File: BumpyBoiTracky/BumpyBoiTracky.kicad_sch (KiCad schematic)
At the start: 0 parts

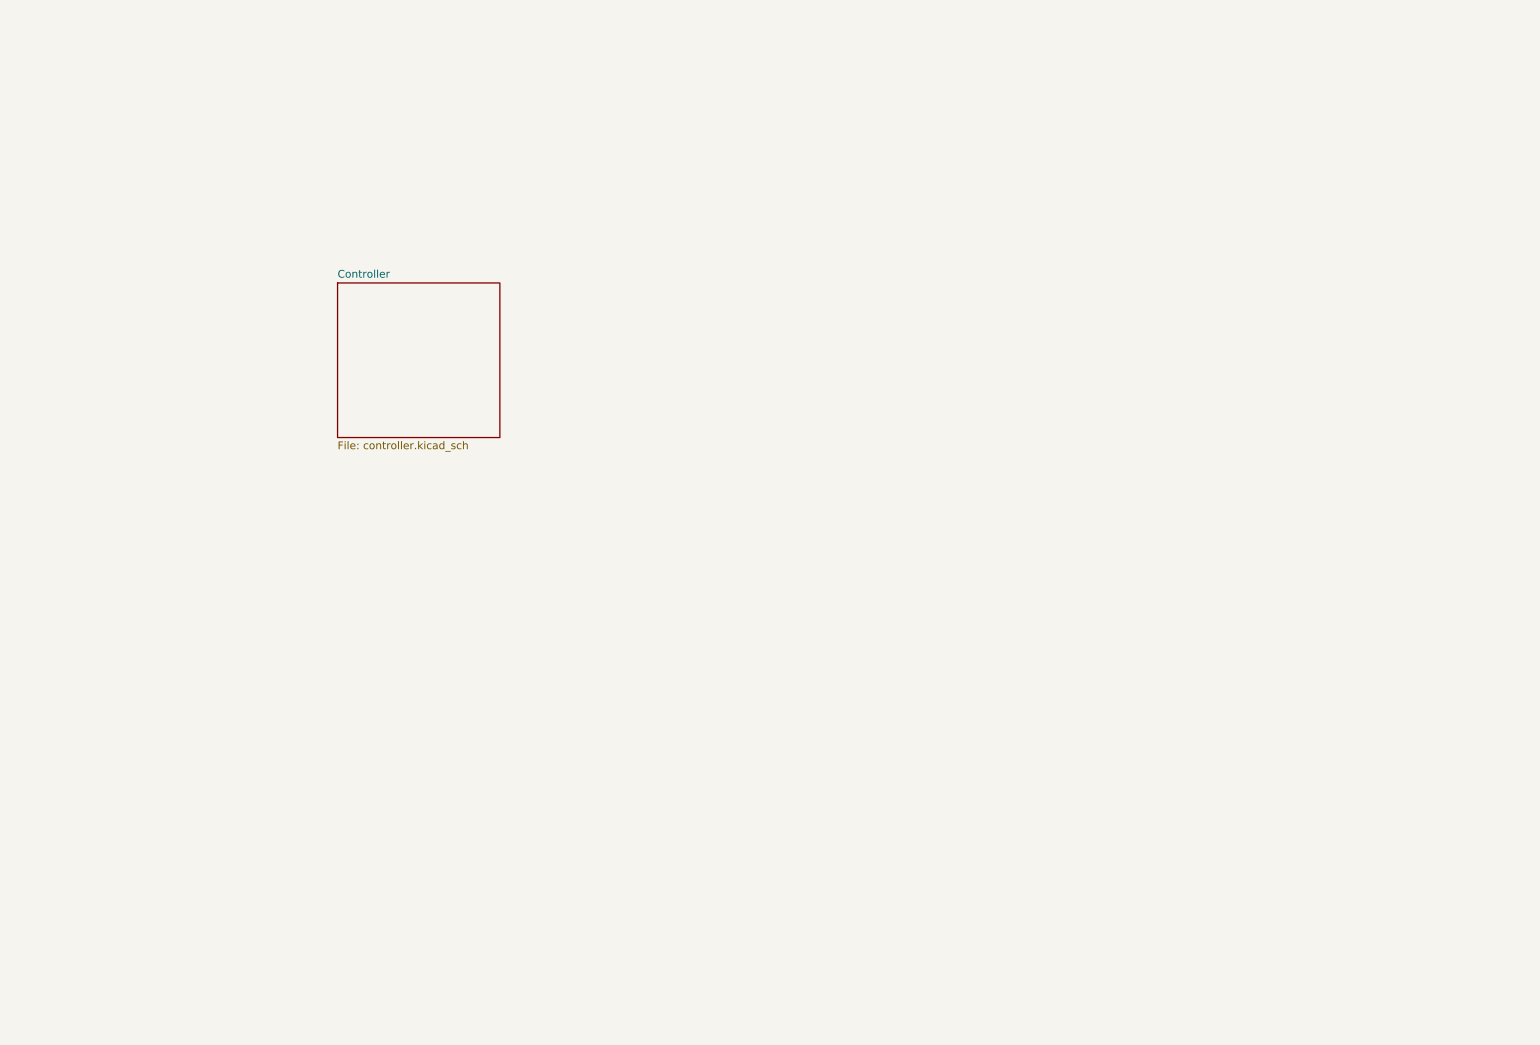
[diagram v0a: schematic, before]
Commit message: Controller Added
Added controller and Sensor. Begun work on prog interface
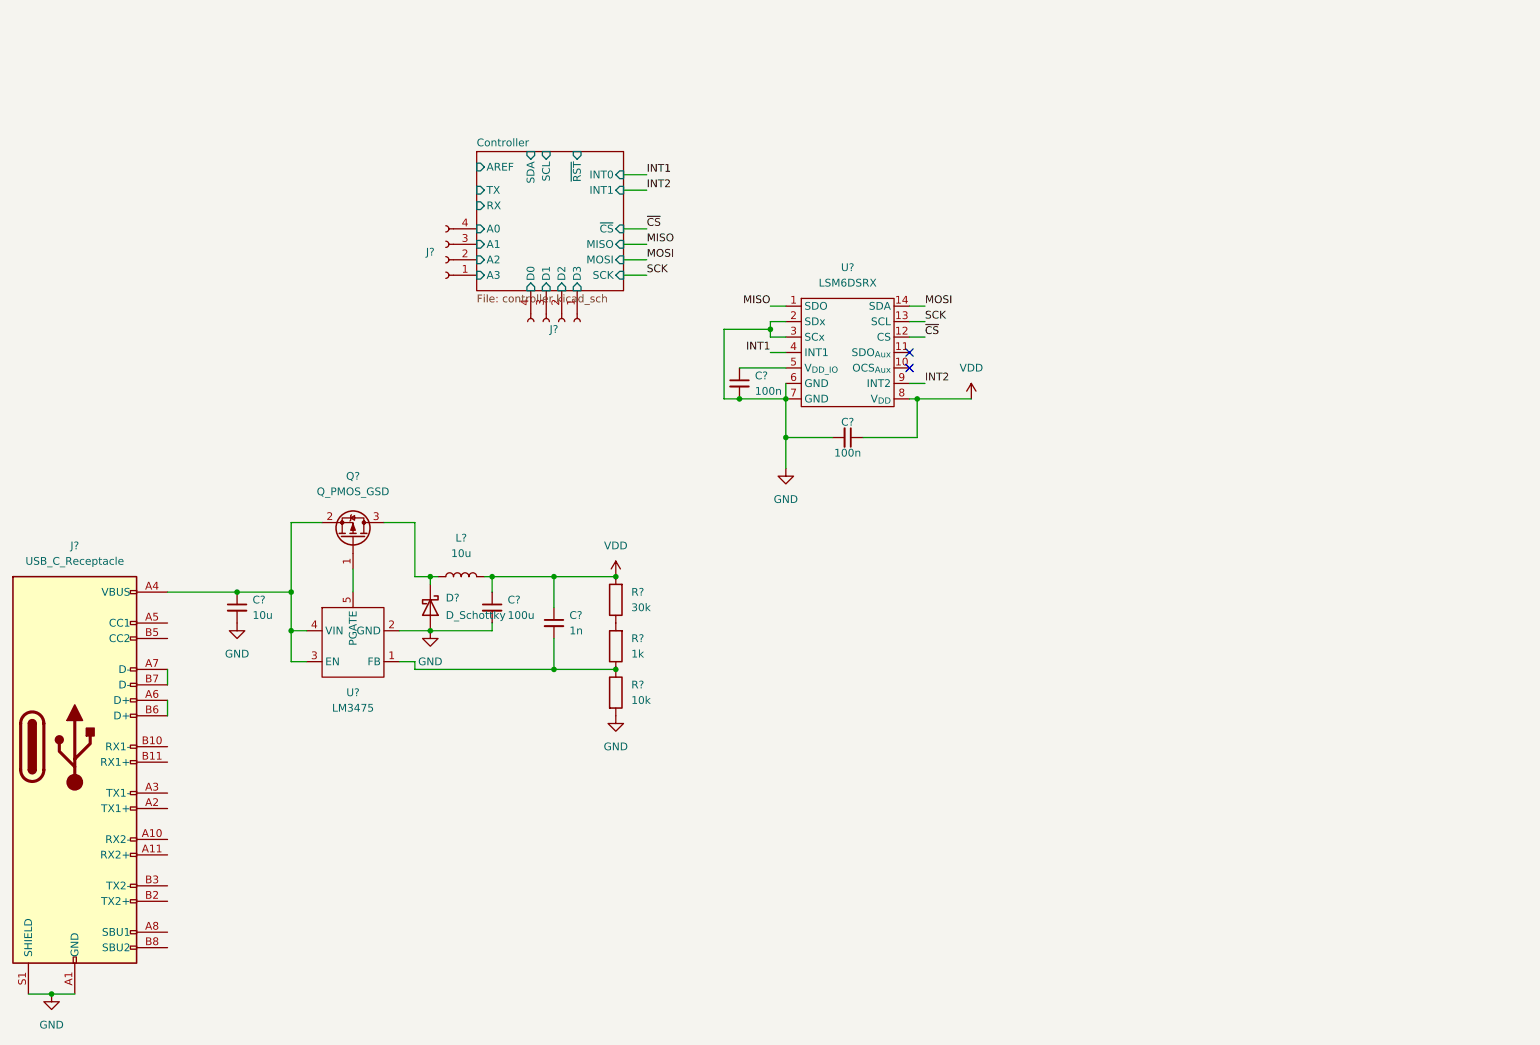
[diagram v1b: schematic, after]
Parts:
- added C?: 1n, symbol Device:C_Small
- added C? (x2): 100n, symbol Device:C_Small
- added C?: 100u, symbol Device:C_Small
- added C?: 10u, symbol Device:C_Small
- added D?: D_Schottky, symbol Device:D_Schottky
- added J?: USB_C_Receptacle, symbol Connector:USB_C_Receptacle
- added J? (x2): Conn_01x04_Female, symbol Connector:Conn_01x04_Female
- added L?: 10u, symbol Device:L
- added Q?: Q_PMOS_GSD, symbol Device:Q_PMOS_GSD
- added R?: 30k, symbol Device:R
- added R?: 1k, symbol Device:R
- added R?: 10k, symbol Device:R
- added U?: LM3475, Package_TO_SOT_SMD:SOT-23-5, symbol BumpyBoiTracky:LM3475
- added U?: LSM6DSRX, BumpyBoiTracky:LGA-14L, symbol BumpyBoiTracky:LSM6DSRX
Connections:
- new net: R?.1, R?.2
- new net: C?.2, R?.1, R?.1, U?.1 (FB)
- new net: C?.1, U?.5 (V_{DD_IO})
- new net: C?.1, J?.A4 (VBUS), J?.A9 (VBUS), J?.B4 (VBUS), J?.B9 (VBUS), Q?.2 (S), U?.3 (EN), U?.4 (VIN)
- new net: Q?.1 (G), U?.5 (PGATE)
- new net: D?.1 (K), L?.1, Q?.3 (D)
- new net: J?.A6 (D+), J?.B6 (D+)
- new net: J?.A7 (D-), J?.B7 (D-)
- new net Controller/A0: J?.4 (Pin_4)
- new net Controller/A1: J?.3 (Pin_3)
- new net Controller/A2: J?.2 (Pin_2)
- new net Controller/A3: J?.1 (Pin_1)
- new net Controller/D0: J?.4 (Pin_4)
- new net Controller/D1: J?.3 (Pin_3)
- new net Controller/D2: J?.2 (Pin_2)
- new net Controller/D3: J?.1 (Pin_1)
- new net GND: C?.2, C?.2, C?.2, C?.2, D?.2 (A), J?.A1 (GND), J?.A12 (GND), J?.B1 (GND), J?.B12 (GND), J?.S1 (SHIELD), R?.2, U?.2 (GND), U?.2 (SDx), U?.3 (SCx), U?.6 (GND), U?.7 (GND)
- new net INT1: U?.4 (INT1)
- new net INT2: U?.9 (INT2)
- new net MISO: U?.1 (SDO)
- new net MOSI: U?.14 (SDA)
- new net SCK: U?.13 (SCL)
- new net VDD: C?.1, C?.1, C?.1, L?.2, R?.2, U?.8 (V_{DD})
- new net ~{CS}: U?.12 (CS)
- no-connect marks 0 -> 2
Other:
- sheet Controller ports: added A0, A1, A2, A3, AREF, D0, D1, D2, D3, INT0, INT1, MISO, MOSI, RX, SCK, SCL, SDA, TX, ~{CS}, ~{RST}; removed none

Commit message: (adding forgotten files)
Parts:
- removed C?: 1n, symbol Device:C_Small
- removed C? (x2): 100n, symbol Device:C_Small
- removed C?: 100u, symbol Device:C_Small
- removed C?: 10u, symbol Device:C_Small
- removed D?: D_Schottky, symbol Device:D_Schottky
- removed J?: Conn_01x04_Female, symbol Connector:Conn_01x04_Female
- removed L?: 10u, symbol Device:L
- removed Q?: Q_PMOS_GSD, symbol Device:Q_PMOS_GSD
- removed R?: 30k, symbol Device:R
- removed R?: 1k, symbol Device:R
- removed R?: 10k, symbol Device:R
- removed U?: LM3475, Package_TO_SOT_SMD:SOT-23-5, symbol BumpyBoiTracky:LM3475
- removed U?: LSM6DSRX, BumpyBoiTracky:LGA-14L, symbol BumpyBoiTracky:LSM6DSRX
- added J2: Conn_01x04_Female, Connector_PinHeader_2.54mm:PinHeader_1x04_P2.54mm_Vertical, symbol Connector:Conn_01x04_Female
- added R1, R4: 1.5k, Resistor_SMD:R_0603_1608Metric, symbol Device:R
- added R2: 36k, Resistor_SMD:R_0603_1608Metric, symbol Device:R
- added R3, R5: 15k, Resistor_SMD:R_0603_1608Metric, symbol Device:R
- added SW1: RST Switch, symbol Switch:SW_Push
- J3: renamed from J?; footprint (none) -> Connector_PinHeader_2.54mm:PinHeader_1x04_P2.54mm_Vertical
- gave numbers to parts that had none: 1
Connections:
- net Controller/A0: now also J2.4 (Pin_4)
- net Controller/A1: now also J2.3 (Pin_3)
- net Controller/A2: now also J2.2 (Pin_2)
- net Controller/A3: now also J2.1 (Pin_1)
- net Controller/~{RST}: now also R1.2, SW1.1
- net GND: now also R3.2, R5.2, SW1.2
- net Voltage Converters/V_{in}: now reaches J1.A4 (VBUS), J1.A9 (VBUS), J1.B4 (VBUS), J1.B9 (VBUS)
- net USB_CC1: now reaches J1.A5 (CC1)
- net USB_CC1: now also R2.1
- net USB_D+: now reaches J1.A6 (D+), J1.B6 (D+)
- net USB_D+: now also R4.2, R5.1
- net USB_D-: now reaches J1.A7 (D-), J1.B7 (D-)
- net USB_D-: now also R3.1
- net USB_CC2: now reaches J1.B5 (CC2)
- net USB_CC2: now also R2.2
- new net +3.3V: R4.1
- new net +5V: R1.1
- no-connect marks 2 -> 0
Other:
- added sheet Gyro (gyro.kicad_sch)
- added sheet Voltage Converters (converter.kicad_sch)
- sheet Controller ports: added PB0, PB1, PE0, PE1, PE2, PE3, VDD, VDDA; removed none
- note added: "USB Connections"
- moved on the sheet: J3

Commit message: Began layout for circuit board
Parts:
- J1: footprint (none) -> BumpyBoiTracky:Amphenol_USB-C_10164359-00011LF
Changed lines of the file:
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@@
     (property "Reference" "J1" (id 0) (at 43.18 107.95 0))
     (property "Value" "USB_C_Receptacle" (id 1) (at 43.18 110.49 0))
-    (property "Footprint" "" (id 2) (at 46.99 140.97 0)
+    (property "Footprint" "BumpyBoiTracky:Amphenol_USB-C_10164359-00011LF" (id 2) (at 46.99 140.97 0)
       (effects (font (size 1.27 1.27)) hide)
     )
@@
     )
     (path "/a50771fd-69e1-4805-ba66-c397618a482a"
-      (reference "J1") (unit 1) (value "USB_C_Receptacle") (footprint "")
+      (reference "J1") (unit 1) (value "USB_C_Receptacle") (footprint "BumpyBoiTracky:Amphenol_USB-C_10164359-00011LF")
     )
     (path "/dbbc42e1-14d2-46e9-8990-1711bd3e37a5"
